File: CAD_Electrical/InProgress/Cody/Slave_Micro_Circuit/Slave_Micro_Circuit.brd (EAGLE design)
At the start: 36.5 x 82.5 mm, 22 parts, among them IC1 ATMEGA88A-PU, IC2 TS12A4515P, IC3 TS12A4515P, IC4 TS12A4515P, J1 22-23-2061, Y1 16MHz

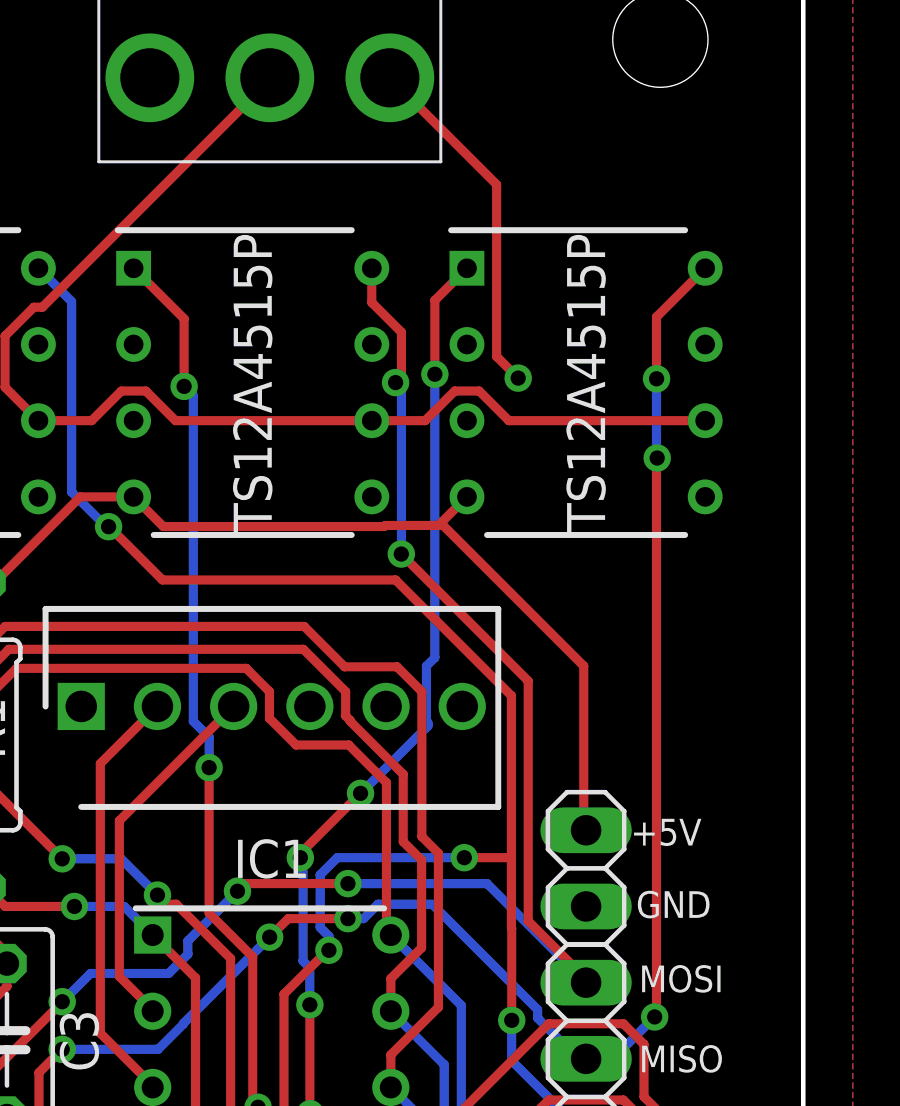
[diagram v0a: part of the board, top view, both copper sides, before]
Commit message: Created slave micro Eagle component.
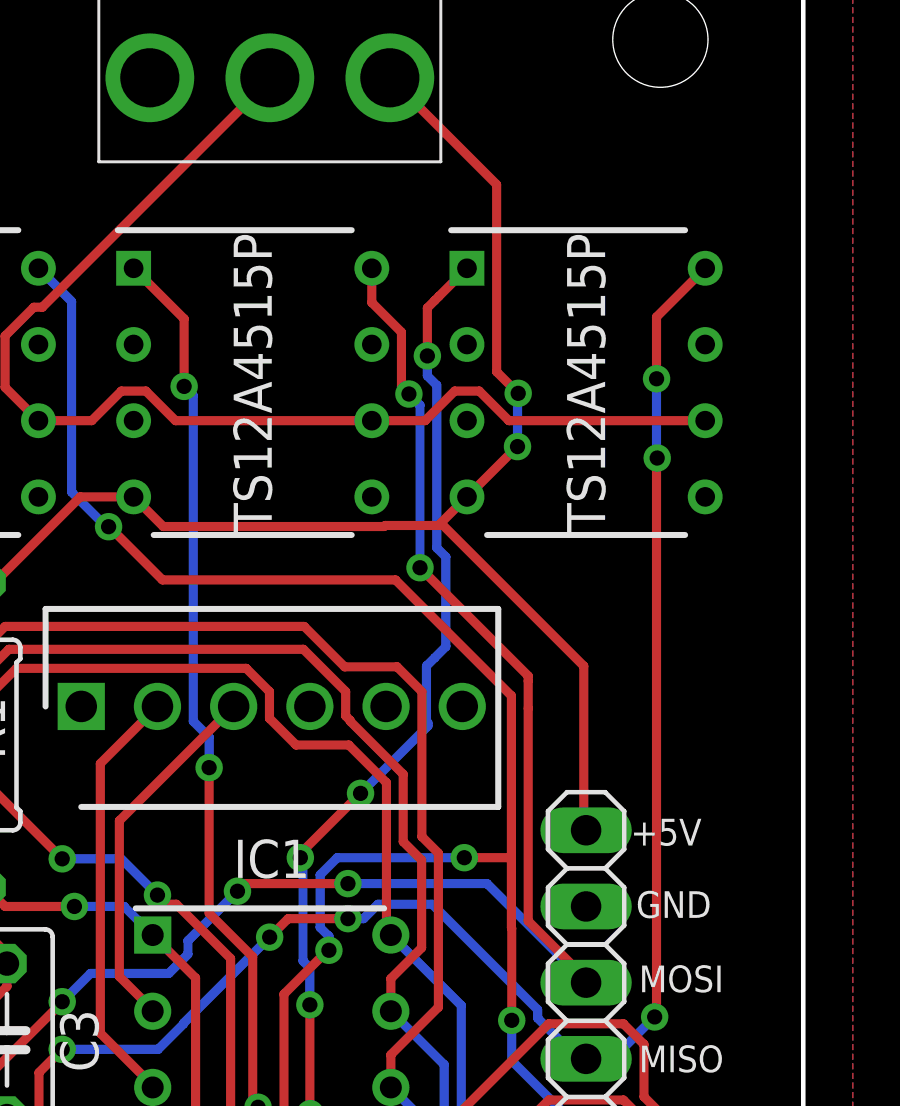
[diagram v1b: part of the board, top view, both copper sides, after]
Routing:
- net +5V: track 140.2 -> 144.9 mm, vias 3 -> 4
- net MISO: track 66.9 -> 67.5 mm
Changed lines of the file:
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@@
 <?xml version="1.0" encoding="utf-8"?>
 <!DOCTYPE eagle SYSTEM "eagle.dtd">
-<eagle version="9.3.0">
+<eagle version="9.6.2">
 <drawing>
 <settings>
@@
 <wire x1="22.57560625" y1="61.6585" x2="24.351" y2="61.6585" width="0.3048" layer="1"/>
 <wire x1="22.732" y1="76.581" x2="26.2914" y2="73.0216" width="0.3048" layer="1"/>
-<wire x1="26.2914" y1="67.289525" x2="27.0102125" y2="66.5707125" width="0.3048" layer="1"/>
-<via x="27.0102125" y="66.5707125" extent="1-16" drill="0.508"/>
-<wire x1="26.2914" y1="73.0216" x2="26.2914" y2="67.289525" width="0.3048" layer="1"/>
+<wire x1="26.2914" y1="66.781525" x2="27.0102125" y2="66.0627125" width="0.3048" layer="1"/>
+<via x="27.0102125" y="66.0627125" extent="1-16" drill="0.508"/>
+<wire x1="26.2914" y1="73.0216" x2="26.2914" y2="66.781525" width="0.3048" layer="1"/>
 <wire x1="5.207" y1="43.053" x2="6.731" y2="43.053" width="0.3048" layer="1"/>
 <wire x1="9.27865625" y1="54.66584375" x2="9.277725" y2="54.666775" width="0.3048" layer="1"/>
@@
 <wire x1="29.2735" y1="51.4985" x2="29.1974" y2="51.5746" width="0.3048" layer="1"/>
 <wire x1="29.1974" y1="56.9721" x2="24.431" y2="61.7385" width="0.3048" layer="1"/>
-<wire x1="25.3035" y1="62.611" x2="27.0102125" y2="66.5707125" width="0" layer="19" extent="1-1"/>
+<wire x1="25.3035" y1="62.611" x2="26.9799" y2="64.2874" width="0.3048" layer="1"/>
+<wire x1="26.9799" y1="64.2874" x2="26.9875" y2="64.2874" width="0.3048" layer="1"/>
+<via x="26.9875" y="64.2874" extent="1-16" drill="0.508"/>
+<wire x1="26.9875" y1="64.2874" x2="26.9875" y2="66.04" width="0.3048" layer="16"/>
+<wire x1="26.9875" y1="66.04" x2="27.0102125" y2="66.0627125" width="0.3048" layer="16"/>
 </signal>
 <signal name="PRESSURE1">
@@
 <wire x1="22.765" y1="21.749" x2="21.082" y2="20.066" width="0.3048" layer="1"/>
 <contactref element="IC4" pad="1"/>
-<wire x1="25.3035" y1="70.231" x2="24.2330375" y2="69.1605375" width="0.3048" layer="1"/>
-<wire x1="24.2330375" y1="69.1605375" x2="24.2330375" y2="66.6989625" width="0.3048" layer="1"/>
-<via x="24.2330375" y="66.6989625" extent="1-16" drill="0.508"/>
-<wire x1="24.2330375" y1="66.6989625" x2="24.2330375" y2="57.2530375" width="0.3048" layer="16"/>
+<wire x1="25.3035" y1="70.231" x2="24.3675" y2="69.295" width="0.3048" layer="1"/>
+<wire x1="24.3675" y1="69.295" x2="24.2330375" y2="69.1605375" width="0.3048" layer="1"/>
 <wire x1="24.003" y1="54.97618125" x2="21.7551" y2="52.72828125" width="0.3048" layer="16"/>
 <via x="21.7551" y="52.72828125" extent="1-16" drill="0.508"/>
 <wire x1="23.9521" y1="55.13146875" x2="24.003" y2="55.08056875" width="0.3048" layer="16"/>
 <wire x1="24.003" y1="55.08056875" x2="24.003" y2="54.97618125" width="0.3048" layer="16"/>
-<wire x1="24.2330375" y1="57.2530375" x2="23.9521" y2="56.9721" width="0.3048" layer="16"/>
+<wire x1="24.2330375" y1="57.2530375" x2="23.97125" y2="56.99125" width="0.3048" layer="16"/>
+<wire x1="23.97125" y1="56.99125" x2="23.9521" y2="56.9721" width="0.3048" layer="16"/>
 <wire x1="23.9521" y1="56.9721" x2="23.9521" y2="55.13146875" width="0.3048" layer="16"/>
 <wire x1="21.7551" y1="52.72828125" x2="19.7485" y2="50.72168125" width="0.3048" layer="1"/>
@@
 <wire x1="22.7965" y1="22.66813125" x2="20.268528125" y2="25.196103125" width="0.3048" layer="16"/>
 <wire x1="20.268528125" y1="25.196103125" x2="20.268528125" y2="25.323103125" width="0.3048" layer="16"/>
+<wire x1="24.2330375" y1="69.1605375" x2="23.9825" y2="68.91" width="0.3048" layer="1"/>
+<wire x1="23.9825" y1="68.91" x2="23.9825" y2="67.31" width="0.3048" layer="1"/>
+<via x="23.9825" y="67.31" extent="1-16" drill="0.508"/>
+<wire x1="23.9825" y1="67.31" x2="23.9825" y2="66.64681875" width="0.3048" layer="16"/>
+<wire x1="24.29616875" y1="60.91238125" x2="24.60096875" y2="60.60758125" width="0.3048" layer="16"/>
+<wire x1="23.9825" y1="66.64681875" x2="24.29616875" y2="66.33315" width="0.3048" layer="16"/>
+<wire x1="24.29616875" y1="66.33315" x2="24.29616875" y2="60.91238125" width="0.3048" layer="16"/>
+<wire x1="24.60096875" y1="60.60758125" x2="24.60096875" y2="57.62096875" width="0.3048" layer="16"/>
+<wire x1="24.60096875" y1="57.62096875" x2="24.2330375" y2="57.2530375" width="0.3048" layer="16"/>
 </signal>
 <signal name="SCK">
@@
 <contactref element="JP4" pad="1"/>
 <contactref element="JP3" pad="1"/>
-<via x="23.114" y="60.706" extent="1-16" drill="0.508"/>
 <wire x1="29.2735" y1="46.4185" x2="29.2735" y2="46.54413125" width="0.3048" layer="1"/>
 <wire x1="29.2735" y1="46.54413125" x2="27.3431" y2="48.47453125" width="0.3048" layer="1"/>
-<wire x1="27.3431" y1="56.4769" x2="23.114" y2="60.706" width="0.3048" layer="1"/>
-<wire x1="27.3431" y1="48.47453125" x2="27.3431" y2="56.4769" width="0.3048" layer="1"/>
-<wire x1="23.114" y1="60.706" x2="23.1189" y2="60.7109" width="0.3048" layer="16"/>
-<wire x1="23.1189" y1="60.7109" x2="23.1189" y2="66.2256" width="0.3048" layer="16"/>
-<wire x1="23.1189" y1="66.2256" x2="22.9235" y2="66.421" width="0.3048" layer="16"/>
-<via x="22.9235" y="66.421" extent="1-16" drill="0.508"/>
-<wire x1="23.1189" y1="68.10020625" x2="23.1189" y2="66.6164" width="0.3048" layer="1"/>
-<wire x1="22.9235" y1="66.421" x2="23.1189" y2="66.6164" width="0.3048" layer="1"/>
+<wire x1="27.3431" y1="48.47453125" x2="27.3431" y2="55.5625" width="0.3048" layer="1"/>
+<wire x1="27.3431" y1="55.5625" x2="27.3431" y2="56.4769" width="0.3048" layer="1"/>
 <wire x1="22.131" y1="69.08810625" x2="22.131" y2="70.231" width="0.3048" layer="1"/>
-<wire x1="23.1189" y1="68.10020625" x2="22.131" y2="69.08810625" width="0.3048" layer="1"/>
+<wire x1="22.131" y1="69.08810625" x2="23.1189" y2="68.10020625" width="0.3048" layer="1"/>
 <via x="7.4295" y="39.6875" extent="1-16" drill="0.508"/>
 <wire x1="7.2009" y1="39.4589" x2="7.4295" y2="39.6875" width="0.3048" layer="16"/>
@@
 <wire x1="29.2735" y1="46.4185" x2="25.9715" y2="49.7205" width="0.3048" layer="16"/>
 <wire x1="21.336" y1="49.7205" x2="25.9715" y2="49.7205" width="0.3048" layer="16"/>
+<wire x1="23.1189" y1="68.10020625" x2="23.1189" y2="66.2891" width="0.3048" layer="1"/>
+<wire x1="23.1189" y1="66.2891" x2="23.368" y2="66.04" width="0.3048" layer="1"/>
+<via x="23.368" y="66.04" extent="1-16" drill="0.508"/>
+<wire x1="23.368" y1="66.04" x2="23.737359375" y2="65.670640625" width="0.3048" layer="16"/>
+<wire x1="23.737359375" y1="65.670640625" x2="23.737359375" y2="60.249859375" width="0.3048" layer="16"/>
+<via x="23.737359375" y="60.249859375" extent="1-16" drill="0.508"/>
+<wire x1="23.737359375" y1="60.249859375" x2="27.3431" y2="56.64411875" width="0.3048" layer="1"/>
+<wire x1="27.3431" y1="56.64411875" x2="27.3431" y2="56.4769" width="0.3048" layer="1"/>
 </signal>
 <signal name="MISO_OUT">
